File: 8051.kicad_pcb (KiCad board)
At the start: 2 copper layers, 40.8 x 78.8 mm, 34 parts, among them J1 Conn_01x02_Male, J2 Conn_02x30_Odd_Even, J3 Conn_01x02_Male, J4 Conn_01x02_Male, J5 Conn_01x01_Male, SW1 SW_Push, U1 P87C51RB, U2 74HC244, U3 74LS373, U4 74LS373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

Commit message: convert to new Kicad, replace led, add uart header
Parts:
- added D5: LED, LED_SMD:LED_0805_2012Metric_Pad1.15x1.40mm_HandSolder, F.Cu at (103.5, 118.0)
- added D6: LED, LED_SMD:LED_0805_2012Metric_Pad1.15x1.40mm_HandSolder, F.Cu at (106.6, 118.0)
- added J6: Conn_01x04, Connector_PinHeader_2.54mm:PinHeader_1x04_P2.54mm_Horizontal, F.Cu at (127.3, 73.9)
- D2: value LED_RCBG -> LED; footprint LED_THT:LED_D5.0mm-4_RGB_Wide_Pins -> LED_SMD:LED_0805_2012Metric_Pad1.15x1.40mm_HandSolder
- moved D2 4.91 mm to (100.6, 118.0), turned to 90 degrees
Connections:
- D2 pad 1: Net-(D2-Pad1) -> GND
- D2 pad 2: GND -> Net-(D2-A)
- R4 pad 1: Net-(D2-Pad3) -> Net-(D5-A)
- R5 pad 1: Net-(D2-Pad4) -> Net-(D2-A)
- R6 pad 1: Net-(D2-Pad1) -> Net-(D6-A)
- U1 pad 1: Net-(U1-Pad1) -> unconnected-(U1-NC-Pad1)
- U1 pad 12: Net-(U1-Pad12) -> unconnected-(U1-NC-Pad12)
- U1 pad 23: Net-(U1-Pad23) -> unconnected-(U1-NC-Pad23)
- U1 pad 34: Net-(U1-Pad34) -> unconnected-(U1-NC-Pad34)
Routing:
- net GND: track 414.9 -> 454.1 mm
- net TxD: track 29.1 -> 46.2 mm, vias 0 -> 2
- net RxD: track 32.6 -> 46.5 mm, vias 0 -> 2
- net Net-(D2-Pad4): track 7.02 -> 0.00 mm
- net Net-(D2-A): track 0.00 -> 6.68 mm
- net Net-(D5-A): track 0.00 -> 6.58 mm, vias 0 -> 1
- net Net-(D6-A): track 0.00 -> 3.47 mm, vias 0 -> 1
- net +5V: track 236.5 -> 233.4 mm
- net T1: track 21.6 -> 24.0 mm
- net Net-(D2-Pad3): track 2.24 -> 0.00 mm
- net Net-(D2-Pad1): track 2.24 -> 0.00 mm
- net T0: track 22.4 -> 24.3 mm
- net INT0: track 27.0 -> 28.4 mm
- net INT1: track 26.2 -> 27.5 mm
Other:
- net class Default removed
- board text added: "--->"
- board text added: "1"
- board text added: "2"
- board text added: "G T R 5"
- board text added: "plpg version '24 rev 1"
- board text removed: "-->"

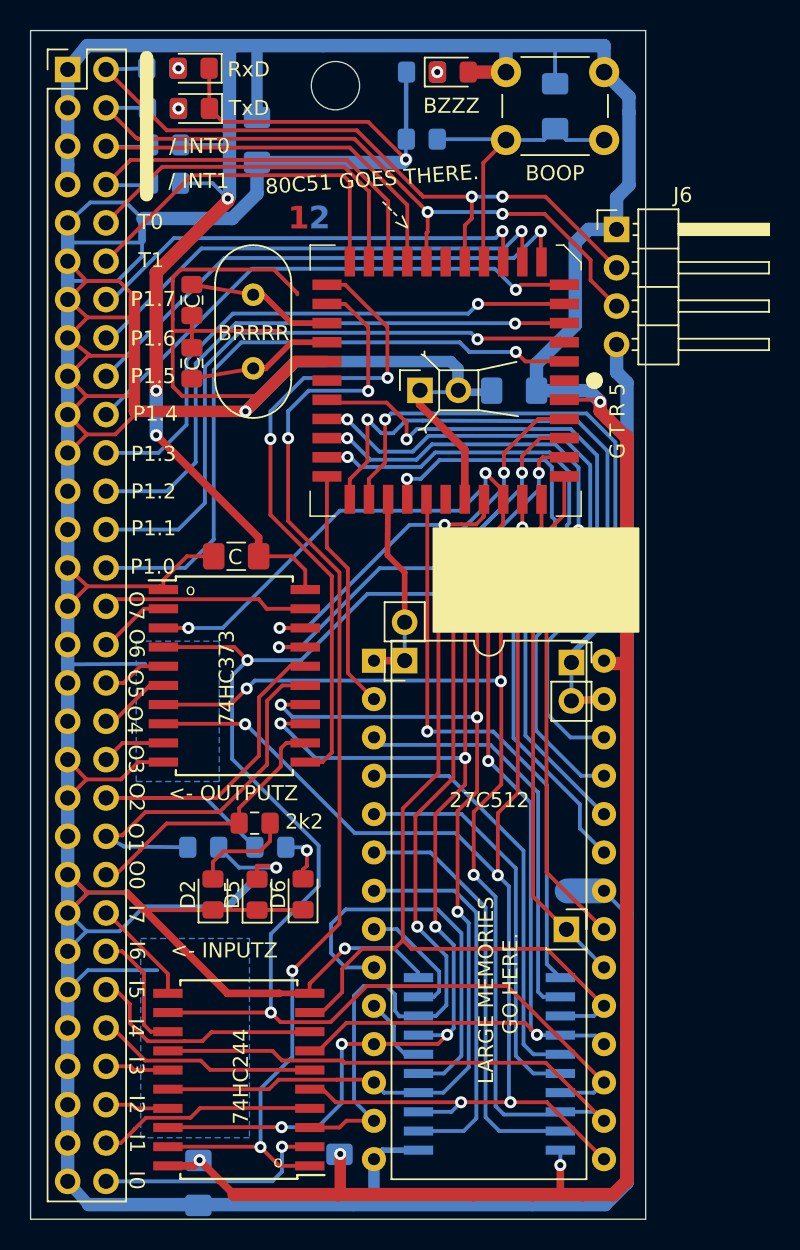
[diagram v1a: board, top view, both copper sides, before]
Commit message: implement rue's errata; update to Kicad 8; revision 2
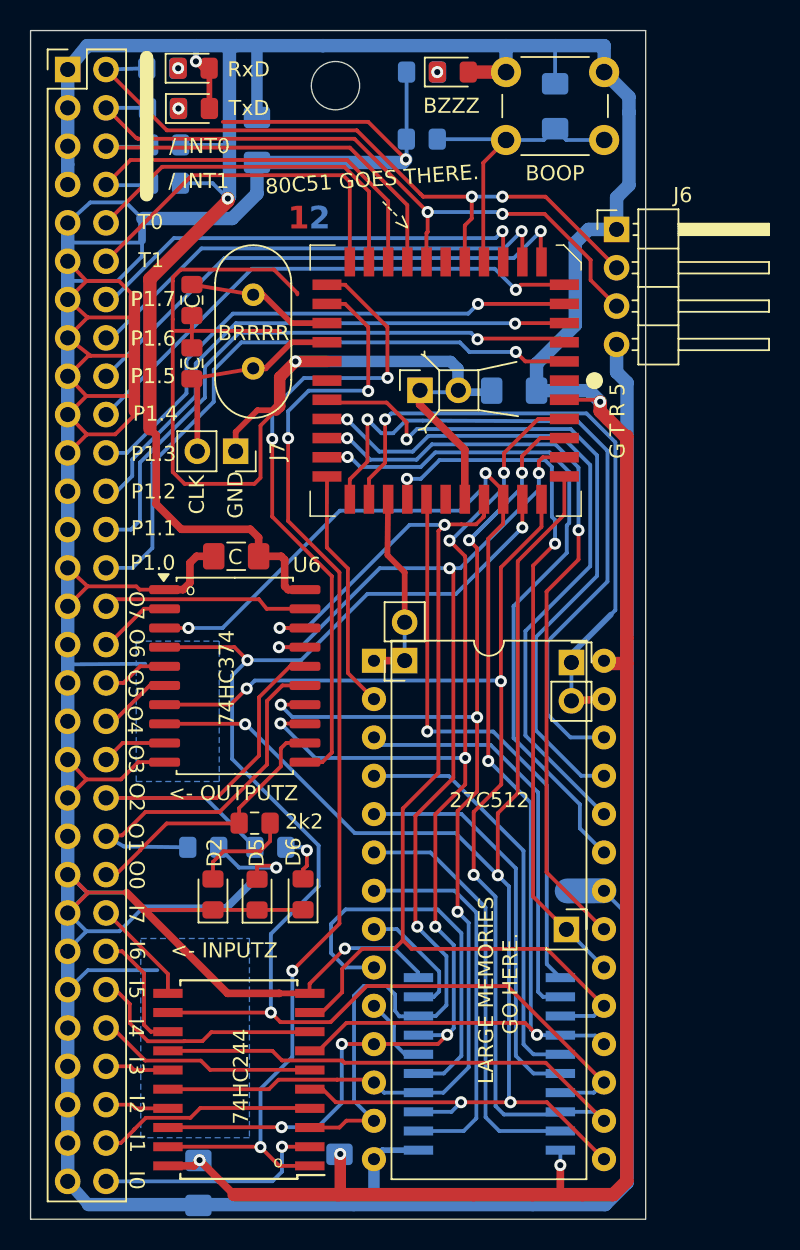
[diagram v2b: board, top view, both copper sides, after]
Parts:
- removed U3: 74LS373, Package_SO:SOIC-20W_7.5x12.8mm_P1.27mm
- added G***: LOGO, LOGO, B.Cu at (120.1, 111.6)
- added J7: EXTCLK, Connector_PinSocket_2.54mm:PinSocket_1x02_P2.54mm_Vertical, F.Cu at (102.1, 88.6)
- added U6: 74LS374, Package_SO:SOIC-20W_7.5x12.8mm_P1.27mm, F.Cu at (102.0, 103.5)
- turned D3 to 0 degrees
- turned D4 to 0 degrees
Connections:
- D3 pad 1: GND -> Net-(D3-K)
- D3 pad 2: Net-(D3-A) -> +5V
- D4 pad 1: GND -> Net-(D4-K)
- D4 pad 2: Net-(D4-A) -> +5V
- R1 pad 1: Net-(D3-A) -> Net-(D3-K)
- R7 pad 1: Net-(D4-A) -> Net-(D4-K)
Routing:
- net +5V: track 233.4 -> 241.4 mm, vias 7 -> 6
- net GND: track 454.1 -> 448.4 mm
- net Net-(J7-Pin_2): track 9.73 -> 14.7 mm
- net P0: track 43.7 -> 41.6 mm
- net P2: track 38.8 -> 36.9 mm
- net P1: track 41.3 -> 39.5 mm
- net P3: track 37.0 -> 35.7 mm
- net Net-(D3-K): track 0.00 -> 0.03 mm, vias 0 -> 1
- net Net-(D4-K): vias 0 -> 1
- net Net-(D4-A): vias 1 -> 0
- net Net-(D3-A): vias 1 -> 0
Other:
- board text added: "74HC374"
- board text added: "CLK"
- board text added: "plpg version '24 rev 2"
- board text removed: "plpg version '24 rev 1"
